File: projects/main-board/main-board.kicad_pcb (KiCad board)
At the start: 4 copper layers, 215 parts, among them J1 TC2030, J2 TC2030, J3 S3B-PH-SM4-TB, J4 USB4105-GF-A, J5 TC2030, J6 NHD-4.3-480272EF-ASXP (Molex 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, J7 USB4105-GF-A, Q1 ZXTN4240F-7, Q2 ZXTN4240F-7, SW1 450404015514, SW10 TS06-667-25-BK-160-G-SMT-TR, SW11 TS06-667-25-BK-160-G-SMT-TR, SW12 TS06-667-25-BK-160-G-SMT-TR, SW13 TS06-667-25-BK-160-G-SMT-TR, SW14 TS06-667-25-BK-160-G-SMT-TR, SW15 TS06-667-25-BK-160-G-SMT-TR, SW16 TS06-667-25-BK-160-G-SMT-TR, SW18 TS06-667-25-BK-160-G-SMT-TR, SW2 TS06-667-25-BK-160-G-SMT-TR, SW3 TS06-667-25-BK-160-G-SMT-TR, SW4 TS06-667-25-BK-160-G-SMT-TR, SW5 TS06-667-25-BK-160-G-SMT-TR, SW6 TS06-667-25-BK-160-G-SMT-TR, SW7 TS06-667-25-BK-160-G-SMT-TR, SW8 TS06-667-25-BK-160-G-SMT-TR, SW9 TS06-667-25-BK-160-G-SMT-TR, U1 STM32N657X0HxQ, U10 AP5725WG-7, U11 NAU8325YG, U12 TLV74330PDBVR, U13 DM3AT-SF-PEJM5, U14 LSM6DSO32TR, U2 APS256XXN-OBR-BG, U3 MX25UM25645GXDI00, U4 TPS22992RXPR, U5 MPM3805GQB-18-Z, U6 TPSM863253RDXR, U7 MAX77972EWX+T, U8 TS3USB221ARSER, U9 ESP32-C6FH4, Y1 ABM10W-40.0000MHZ-8-B1U-T3

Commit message: Update renders.
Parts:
- moved SW18 304.7 mm to (254.0, 53.2), turned to 90 degrees
- moved SW16 293.6 mm to (245.8, 53.2), turned to 90 degrees
- moved SW5 292.7 mm to (213.6, 73.2)
- moved SW14 286.4 mm to (263.3, 108.6)
- moved SW11 286.4 mm to (247.9, 103.6)
- moved SW15 285.4 mm to (263.1, 121.1)
- moved SW10 282.0 mm to (247.9, 115.5)
- moved J4 213.0 mm to (187.5, 34.3), turned to 180 degrees
- moved C87 212.8 mm to (166.6, 66.8), turned to 0 degrees
- moved R55 209.7 mm to (165.1, 70.5), turned to -90 degrees
- moved L6 207.3 mm to (163.7, 63.5), turned to 180 degrees
- moved U10 207.2 mm to (163.8, 67.8), turned to 0 degrees
- moved SW9 203.6 mm to (150.4, 124.3)
- moved R56 201.5 mm to (161.0, 68.7), turned to 180 degrees
- moved R53 200.0 mm to (185.7, 40.9), turned to -90 degrees
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
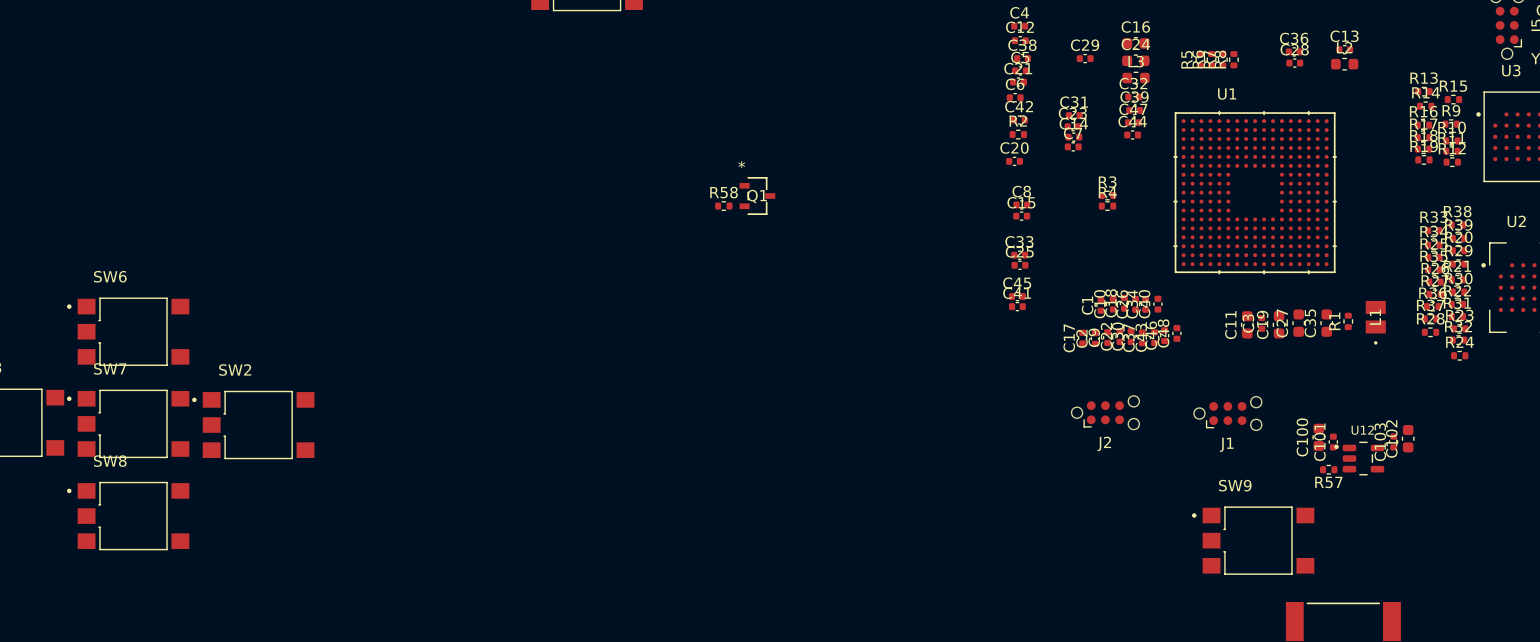
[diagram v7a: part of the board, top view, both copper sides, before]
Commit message: Update images. Add render.
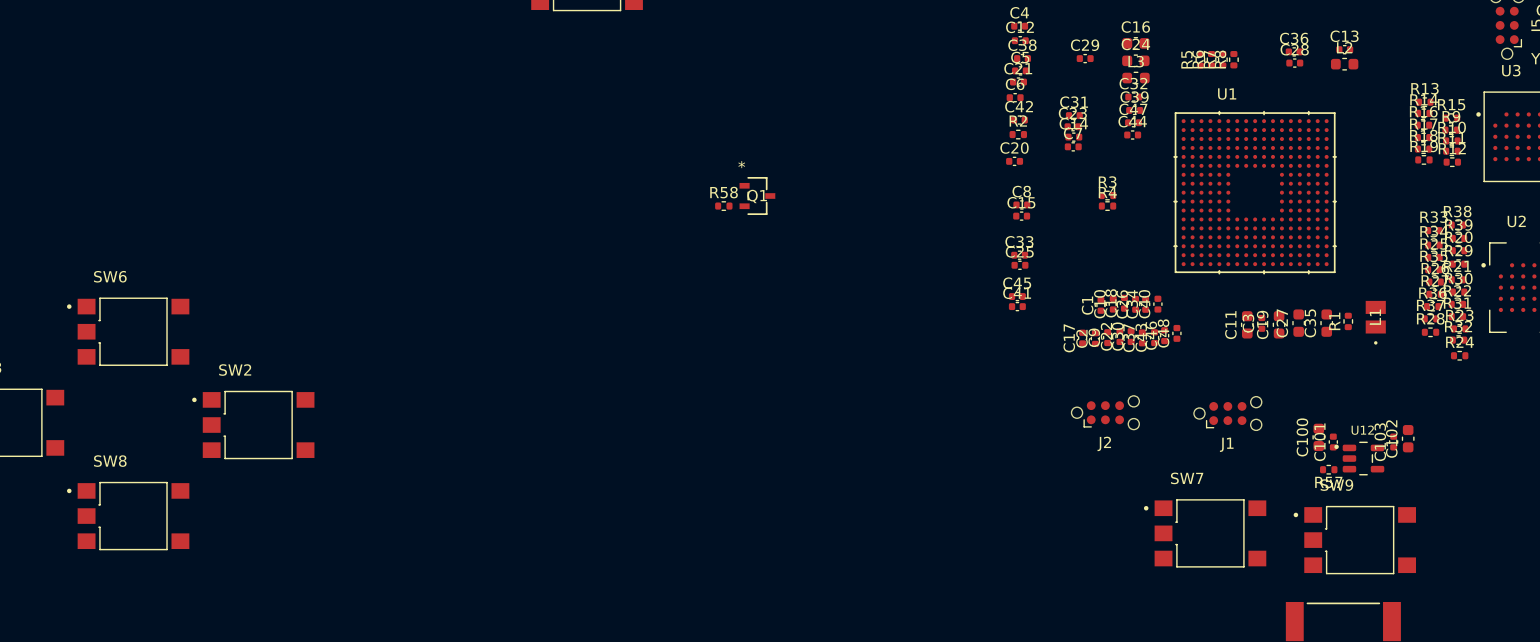
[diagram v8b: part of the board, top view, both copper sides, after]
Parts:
- moved SW7 96.9 mm to (146.1, 123.7)
- moved SW9 9.10 mm to (159.5, 124.3)
- moved R15 1.67 mm to (167.7, 86.5)
- moved R13 0.94 mm to (165.3, 85.1)
- moved R14 0.65 mm to (165.2, 86.1)
- moved R9 0.53 mm to (167.6, 87.6)
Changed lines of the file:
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@@
 	(footprint "Resistor_SMD:R_0402_1005Metric"
 		(layer "F.Cu")
-		(at 167.849998 84.870001)
+		(at 167.680002 86.529999)
 		(descr "Resistor SMD 0402 (1005 Metric), square (rectangular) end terminal, IPC-7351 nominal, (Body size source: IPC-SM-782 page 72, https://www.pcb-3d.com/wordpress/wp-content/uploads/ipc-sm-782a_amendment_1_and_2.pdf), generated with kicad-footprint-generator")
 		(tags "resistor")
@@
 	(footprint "Resistor_SMD:R_0402_1005Metric"
 		(layer "F.Cu")
-		(at 165.369996 85.470002)
+		(at 165.2 86.1)
 		(descr "Resistor SMD 0402 (1005 Metric), square (rectangular) end terminal, IPC-7351 nominal, (Body size source: IPC-SM-782 page 72, https://www.pcb-3d.com/wordpress/wp-content/uploads/ipc-sm-782a_amendment_1_and_2.pdf), generated with kicad-footprint-generator")
 		(tags "resistor")
@@
 	(footprint "Resistor_SMD:R_0402_1005Metric"
 		(layer "F.Cu")
-		(at 167.649998 87.070001)
+		(at 167.649998 87.6)
 		(descr "Resistor SMD 0402 (1005 Metric), square (rectangular) end terminal, IPC-7351 nominal, (Body size source: IPC-SM-782 page 72, https://www.pcb-3d.com/wordpress/wp-content/uploads/ipc-sm-782a_amendment_1_and_2.pdf), generated with kicad-footprint-generator")
 		(tags "resistor")
@@
 	(footprint "footprint-library:TS06-667-25-BK-160-G-SMT-TR"
 		(layer "F.Cu")
-		(at 49.7 113.9)
+		(at 146.1 123.7)
 		(property "Reference" "SW7"
 			(at -2.075 -4.885 0)
@@
 	(footprint "footprint-library:TS06-667-25-BK-160-G-SMT-TR"
 		(layer "F.Cu")
-		(at 150.4 124.35)
+		(at 159.5 124.3)
 		(property "Reference" "SW9"
 			(at -2.075 -4.885 0)
@@
 	(footprint "Resistor_SMD:R_0402_1005Metric"
 		(layer "F.Cu")
-		(at 165.209996 84.160002)
+		(at 165.29 85.1)
 		(descr "Resistor SMD 0402 (1005 Metric), square (rectangular) end terminal, IPC-7351 nominal, (Body size source: IPC-SM-782 page 72, https://www.pcb-3d.com/wordpress/wp-content/uploads/ipc-sm-782a_amendment_1_and_2.pdf), generated with kicad-footprint-generator")
 		(tags "resistor")
